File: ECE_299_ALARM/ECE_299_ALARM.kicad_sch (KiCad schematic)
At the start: 9 parts, among them SW1 SW_Push_Dual, SW2 SW_Push_Dual, SW3 SW_Push_Dual, SW4 SW_Push_Dual, U1 RDA5807M_Module, U2 RPi_Pico_TH, U3 LM386

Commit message: finish schematic
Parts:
- added AE1: Antenna_Loop, symbol Device:Antenna_Loop
- added C1, C2: 470uF, Capacitor_THT:C_Radial_D6.3mm_H11.0mm_P2.50mm, symbol Device:C_Polarized
- added R1: 10k, Resistor_THT:R_Axial_DIN0309_L9.0mm_D3.2mm_P12.70mm_Horizontal, symbol Device:R
- added R2: 8, Resistor_THT:R_Axial_DIN0309_L9.0mm_D3.2mm_P12.70mm_Horizontal, symbol Device:R
- DISP1: footprint (none) -> ECE:OLED_Display_1.3
- LS1: footprint (none) -> Connector_PinHeader_2.54mm:PinHeader_1x02_P2.54mm_Vertical
- SW1, SW2, SW3, SW4: footprint (none) -> Button_Switch_THT:SW_PUSH_6mm_H4.3mm
- U1: footprint ECE:RDA5807M_Module_TH -> ECE:RDA5807M_Module_SM
- U3: footprint (none) -> ECE:Transformer_Block_AVB_03526
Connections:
- net +3.3V: now also DISP1.2 (VDD), U1.5 (VDD)
- net at U1.1 (SDIO): now also U2.31 (GP26/ADC0)
- net at U1.10 (FMIN): now also AE1.1, AE1.2
- net at U1.2 (SCLK): now also U2.32 (GP27/ADC1)
- net GND: now reaches U1.6 (GND)
- net GND: now also DISP1.1 (VSS/GND), SW1.1, SW2.1, SW3.1, SW4.1, U2.3 (GND), U2.38 (GND), U3.2 (-), U3.4 (GND), R1.2, R2.2
- net at U1.8 (LOUT): now also C1.1
- net SW1: now reaches U2.1 (GP0)
- net SW1: now also SW1.4
- net SW2: now reaches U2.2 (GP1)
- net SW2: now also SW2.4
- net at U2.22 (GP17): now also DISP1.7 (CS)
- net at U2.24 (GP18): now also DISP1.3 (SCLK)
- net at U2.25 (GP19): now also DISP1.4 (SDA)
- net at U2.26 (GP20): now also DISP1.6 (DC)
- net at U2.27 (GP21): now also DISP1.5 (RES)
- net SW3: now reaches U2.4 (GP2)
- net SW3: now also SW3.4
- net +5V: now reaches U2.40 (VBUS)
- net +5V: now also U3.6 (V+)
- net SW4: now reaches U2.5 (GP3)
- net SW4: now also SW4.4
- net at LS1.1: now also C2.2
- net at LS1.2: now also R2.1
- net at U3.3 (+): now also C1.2, R1.1
- net at U3.5: now also C2.1
- no-connect marks 14 -> 37
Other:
- moved on the sheet: DISP1, LS1, SW2, SW3, U1, U3

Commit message: add pullups on i2c
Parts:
- added R3, R4: 1k, Resistor_THT:R_Axial_DIN0309_L9.0mm_D3.2mm_P12.70mm_Horizontal, symbol Device:R
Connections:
- net +3.3V: now also R3.1, R4.1
- net at U1.1 (SDIO), U2.31 (GP26/ADC0): now also R4.2
- net at U1.2 (SCLK), U2.32 (GP27/ADC1): now also R3.2

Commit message: fix antenna footprint
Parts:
- AE1: footprint (none) -> Connector_Wire:SolderWire-0.1sqmm_1x01_D0.4mm_OD1mm
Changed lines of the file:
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@@
 			)
 		)
-		(property "Footprint" ""
+		(property "Footprint" "Connector_Wire:SolderWire-0.1sqmm_1x01_D0.4mm_OD1mm"
 			(at 163.83 41.91 0)
 			(effects

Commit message: fix antenna footprint (fr this time) also fix button footprint to be 2
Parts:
- AE1: footprint Connector_Wire:SolderWire-0.1sqmm_1x01_D0.4mm_OD1mm -> Connector_PinHeader_1.00mm:PinHeader_1x02_P1.00mm_Vertical
- SW1, SW2, SW3, SW4: symbol Switch:SW_Push_Dual -> Switch:SW_Push
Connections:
- net SW1: now also SW1.2; no longer SW1.4
- net SW2: now also SW2.2; no longer SW2.4
- net SW3: now also SW3.2; no longer SW3.4
- net SW4: now also SW4.2; no longer SW4.4
- no-connect marks 37 -> 29

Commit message: fix lm386-4 footprint
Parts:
- U3: footprint ECE:Transformer_Block_AVB_03526 -> Package_DIP:DIP-8_W7.62mm
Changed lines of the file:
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@@
 			)
 		)
-		(property "Footprint" "ECE:Transformer_Block_AVB_03526"
+		(property "Footprint" "Package_DIP:DIP-8_W7.62mm"
 			(at 233.68 87.63 0)
 			(effects

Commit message: added pcb files
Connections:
- net GND: now also U2.23 (GND); no longer U2.38 (GND)
- net at R4.2, U2.31 (GP26/ADC0): now also U1.2 (SCLK); no longer U1.1 (SDIO)
- net at R3.2, U2.32 (GP27/ADC1): now also U1.1 (SDIO); no longer U1.2 (SCLK)
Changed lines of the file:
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@@
-	)
-	(no_connect
-		(at 92.71 130.81)
 	)
 	(no_connect
@@
 	)
 	(no_connect
+		(at 100.33 130.81)
+	)
+	(no_connect
 		(at 73.66 118.11)
 	)
 	(no_connect
+		(at 97.79 130.81)
+	)
+	(no_connect
 		(at 163.83 85.09)
 	)
@@
 	)
 	(no_connect
-		(at 97.79 130.81)
-	)
-	(no_connect
 		(at 73.66 102.87)
 	)
@@
 	(wire
 		(pts
+			(xy 132.08 102.87) (xy 132.08 74.93)
+		)
+		(stroke
+			(width 0)
+			(type default)
+		)
+	)
+	(wire
+		(pts
 			(xy 120.65 115.57) (xy 109.22 115.57)
 		)
@@
 	(wire
 		(pts
-			(xy 132.08 102.87) (xy 132.08 69.85)
-		)
-		(stroke
-			(width 0)
-			(type default)
-		)
-	)
-	(wire
-		(pts
 			(xy 171.45 80.01) (xy 212.09 80.01)
 		)
@@
 	(wire
 		(pts
-			(xy 128.27 100.33) (xy 128.27 74.93)
+			(xy 132.08 74.93) (xy 138.43 74.93)
+		)
+		(stroke
+			(width 0)
+			(type default)
+		)
+	)
+	(wire
+		(pts
+			(xy 128.27 69.85) (xy 128.27 100.33)
 		)
 		(stroke
@@
 	(wire
 		(pts
-			(xy 128.27 74.93) (xy 138.43 74.93)
-		)
-		(stroke
-			(width 0)
-			(type default)
-		)
-	)
-	(wire
-		(pts
 			(xy 212.09 87.63) (xy 212.09 96.52)
 		)
@@
 	(wire
 		(pts
-			(xy 132.08 69.85) (xy 138.43 69.85)
+			(xy 128.27 69.85) (xy 138.43 69.85)
 		)
 		(stroke
@@
 	(symbol
 		(lib_id "power:GND")
-		(at 100.33 130.81 0)
+		(at 92.71 130.81 0)
 		(unit 1)
 		(exclude_from_sim no)
@@
 		(dnp no)
 		(fields_autoplaced yes)
-		(property "Reference" "#PWR03"
-			(at 100.33 137.16 0)
+		(property "Reference" "#PWR022"
+			(at 92.71 137.16 0)
 			(effects
 				(font
@@
 		)
 		(property "Value" "GND"
-			(at 100.33 135.89 0)
+			(at 92.71 135.89 0)
 			(effects
 				(font
@@
 		)
 		(property "Footprint" ""
-			(at 100.33 130.81 0)
+			(at 92.71 130.81 0)
 			(effects
 				(font
@@
 		)
 		(property "Datasheet" ""
-			(at 100.33 130.81 0)
+			(at 92.71 130.81 0)
 			(effects
 				(font
@@
 		)
 		(property "Description" "Power symbol creates a global label with name \"GND\" , ground"
-			(at 100.33 130.81 0)
+			(at 92.71 130.81 0)
 			(effects
 				(font
@@
 			(project ""
 				(path "/8a313705-b4dc-439e-ab35-d82e7777793e"
-					(reference "#PWR03")
+					(reference "#PWR022")
 					(unit 1)
 				)

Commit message: Revert "Web app"
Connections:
- net GND: now also U2.38 (GND); no longer U2.23 (GND)
- net at R3.2, U2.32 (GP27/ADC1): now also U1.2 (SCLK); no longer U1.1 (SDIO)
- net at R4.2, U2.31 (GP26/ADC0): now also U1.1 (SDIO); no longer U1.2 (SCLK)
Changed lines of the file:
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@@
+	)
+	(no_connect
+		(at 92.71 130.81)
 	)
 	(no_connect
@@
 	)
 	(no_connect
-		(at 100.33 130.81)
-	)
-	(no_connect
 		(at 73.66 118.11)
 	)
 	(no_connect
+		(at 163.83 85.09)
+	)
+	(no_connect
+		(at 73.66 105.41)
+	)
+	(no_connect
+		(at 231.14 97.79)
+	)
+	(no_connect
+		(at 233.68 97.79)
+	)
+	(no_connect
+		(at 73.66 115.57)
+	)
+	(no_connect
+		(at 109.22 97.79)
+	)
+	(no_connect
+		(at 231.14 82.55)
+	)
+	(no_connect
 		(at 97.79 130.81)
 	)
 	(no_connect
-		(at 163.83 85.09)
-	)
-	(no_connect
-		(at 73.66 105.41)
-	)
-	(no_connect
-		(at 231.14 97.79)
-	)
-	(no_connect
-		(at 233.68 97.79)
-	)
-	(no_connect
-		(at 73.66 115.57)
-	)
-	(no_connect
-		(at 109.22 97.79)
-	)
-	(no_connect
-		(at 231.14 82.55)
-	)
-	(no_connect
 		(at 73.66 102.87)
 	)
@@
 	(wire
 		(pts
-			(xy 132.08 102.87) (xy 132.08 74.93)
-		)
-		(stroke
-			(width 0)
-			(type default)
-		)
-	)
-	(wire
-		(pts
 			(xy 120.65 115.57) (xy 109.22 115.57)
 		)
@@
 	(wire
 		(pts
+			(xy 132.08 102.87) (xy 132.08 69.85)
+		)
+		(stroke
+			(width 0)
+			(type default)
+		)
+	)
+	(wire
+		(pts
 			(xy 171.45 80.01) (xy 212.09 80.01)
 		)
@@
 	(wire
 		(pts
-			(xy 132.08 74.93) (xy 138.43 74.93)
-		)
-		(stroke
-			(width 0)
-			(type default)
-		)
-	)
-	(wire
-		(pts
-			(xy 128.27 69.85) (xy 128.27 100.33)
+			(xy 128.27 100.33) (xy 128.27 74.93)
 		)
 		(stroke
@@
 	(wire
 		(pts
+			(xy 128.27 74.93) (xy 138.43 74.93)
+		)
+		(stroke
+			(width 0)
+			(type default)
+		)
+	)
+	(wire
+		(pts
 			(xy 212.09 87.63) (xy 212.09 96.52)
 		)
@@
 	(wire
 		(pts
-			(xy 128.27 69.85) (xy 138.43 69.85)
+			(xy 132.08 69.85) (xy 138.43 69.85)
 		)
 		(stroke
@@
 	(symbol
 		(lib_id "power:GND")
-		(at 92.71 130.81 0)
+		(at 100.33 130.81 0)
 		(unit 1)
 		(exclude_from_sim no)
@@
 		(dnp no)
 		(fields_autoplaced yes)
-		(property "Reference" "#PWR022"
-			(at 92.71 137.16 0)
+		(property "Reference" "#PWR03"
+			(at 100.33 137.16 0)
 			(effects
 				(font
@@
 		)
 		(property "Value" "GND"
-			(at 92.71 135.89 0)
+			(at 100.33 135.89 0)
 			(effects
 				(font
@@
 		)
 		(property "Footprint" ""
-			(at 92.71 130.81 0)
+			(at 100.33 130.81 0)
 			(effects
 				(font
@@
 		)
 		(property "Datasheet" ""
-			(at 92.71 130.81 0)
+			(at 100.33 130.81 0)
 			(effects
 				(font
@@
 		)
 		(property "Description" "Power symbol creates a global label with name \"GND\" , ground"
-			(at 92.71 130.81 0)
+			(at 100.33 130.81 0)
 			(effects
 				(font
@@
 			(project ""
 				(path "/8a313705-b4dc-439e-ab35-d82e7777793e"
-					(reference "#PWR022")
+					(reference "#PWR03")
 					(unit 1)
 				)

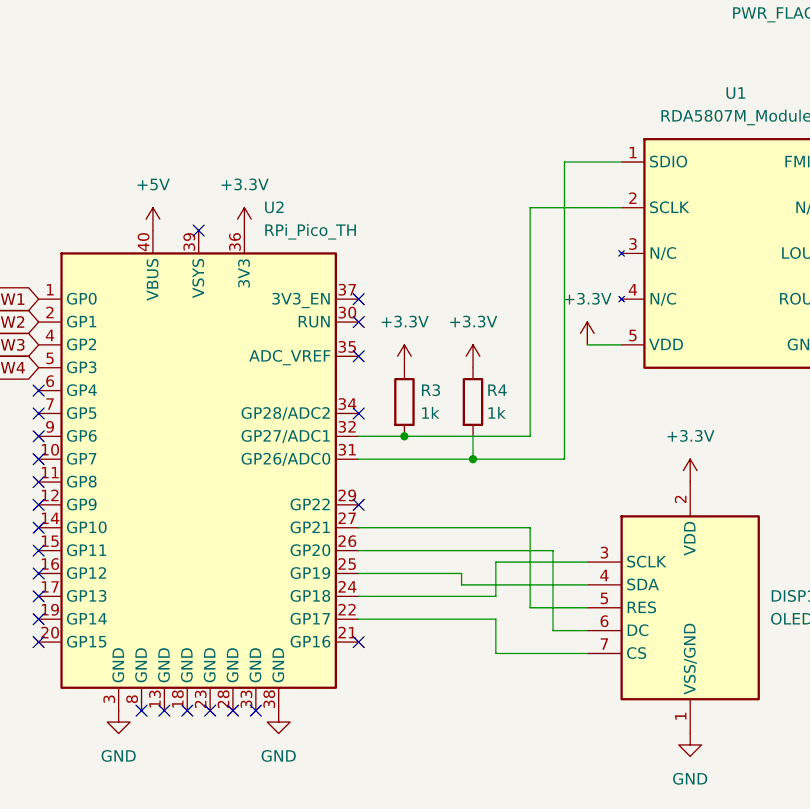
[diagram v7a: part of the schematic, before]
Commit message: error handling for radio and update pcb
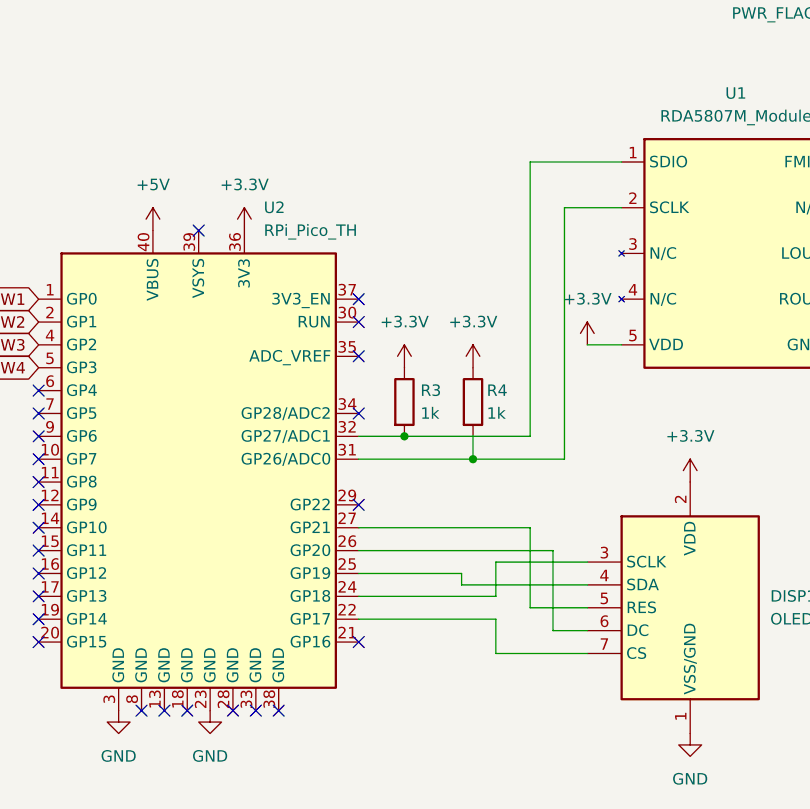
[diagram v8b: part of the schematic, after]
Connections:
- net GND: now also U2.23 (GND); no longer U2.38 (GND)
- net at R4.2, U2.31 (GP26/ADC0): now also U1.2 (SCLK); no longer U1.1 (SDIO)
- net at R3.2, U2.32 (GP27/ADC1): now also U1.1 (SDIO); no longer U1.2 (SCLK)
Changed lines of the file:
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@@
-	)
-	(no_connect
-		(at 92.71 130.81)
 	)
 	(no_connect
@@
 	)
 	(no_connect
+		(at 100.33 130.81)
+	)
+	(no_connect
 		(at 73.66 118.11)
 	)
 	(no_connect
+		(at 97.79 130.81)
+	)
+	(no_connect
 		(at 163.83 85.09)
 	)
@@
 	)
 	(no_connect
-		(at 97.79 130.81)
-	)
-	(no_connect
 		(at 73.66 102.87)
 	)
@@
 	(wire
 		(pts
+			(xy 132.08 102.87) (xy 132.08 74.93)
+		)
+		(stroke
+			(width 0)
+			(type default)
+		)
+	)
+	(wire
+		(pts
 			(xy 120.65 115.57) (xy 109.22 115.57)
 		)
@@
 	(wire
 		(pts
-			(xy 132.08 102.87) (xy 132.08 69.85)
-		)
-		(stroke
-			(width 0)
-			(type default)
-		)
-	)
-	(wire
-		(pts
 			(xy 171.45 80.01) (xy 212.09 80.01)
 		)
@@
 	(wire
 		(pts
-			(xy 128.27 100.33) (xy 128.27 74.93)
+			(xy 132.08 74.93) (xy 138.43 74.93)
+		)
+		(stroke
+			(width 0)
+			(type default)
+		)
+	)
+	(wire
+		(pts
+			(xy 128.27 69.85) (xy 128.27 100.33)
 		)
 		(stroke
@@
 	(wire
 		(pts
-			(xy 128.27 74.93) (xy 138.43 74.93)
-		)
-		(stroke
-			(width 0)
-			(type default)
-		)
-	)
-	(wire
-		(pts
 			(xy 212.09 87.63) (xy 212.09 96.52)
 		)
@@
 	(wire
 		(pts
-			(xy 132.08 69.85) (xy 138.43 69.85)
+			(xy 128.27 69.85) (xy 138.43 69.85)
 		)
 		(stroke
@@
 	(symbol
 		(lib_id "power:GND")
-		(at 100.33 130.81 0)
+		(at 92.71 130.81 0)
 		(unit 1)
 		(exclude_from_sim no)
@@
 		(dnp no)
 		(fields_autoplaced yes)
-		(property "Reference" "#PWR03"
-			(at 100.33 137.16 0)
+		(property "Reference" "#PWR022"
+			(at 92.71 137.16 0)
 			(effects
 				(font
@@
 		)
 		(property "Value" "GND"
-			(at 100.33 135.89 0)
+			(at 92.71 135.89 0)
 			(effects
 				(font
@@
 		)
 		(property "Footprint" ""
-			(at 100.33 130.81 0)
+			(at 92.71 130.81 0)
 			(effects
 				(font
@@
 		)
 		(property "Datasheet" ""
-			(at 100.33 130.81 0)
+			(at 92.71 130.81 0)
 			(effects
 				(font
@@
 		)
 		(property "Description" "Power symbol creates a global label with name \"GND\" , ground"
-			(at 100.33 130.81 0)
+			(at 92.71 130.81 0)
 			(effects
 				(font
@@
 			(project ""
 				(path "/8a313705-b4dc-439e-ab35-d82e7777793e"
-					(reference "#PWR03")
+					(reference "#PWR022")
 					(unit 1)
 				)
